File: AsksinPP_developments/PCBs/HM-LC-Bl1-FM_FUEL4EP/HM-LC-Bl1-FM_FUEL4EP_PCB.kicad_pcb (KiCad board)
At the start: 2 copper layers, 124.5 x 96.7 mm, 68 parts, among them J1 Down Button, J10 charge, J11 24V PSU, J12 230V Netzteil Relais, J13 Velux Motor, J14 Motor direction LEDs, J15 Charge Indication LED, J16 H Brücke Relais In, J17 Motor Relais In, J18 Conn_01x03, J2 Up Button, J3 Dual LED, J4 Config Button, J5 ISP Programmer, J6 Accumulator, J7 LED rot, J8 LED grün, J9 LED gelb, Q1 IRLU024N, Q2 BD238, Q3 IRF9Z34N, Q4 2N7000, Q5 MCP1702-2802E_TO

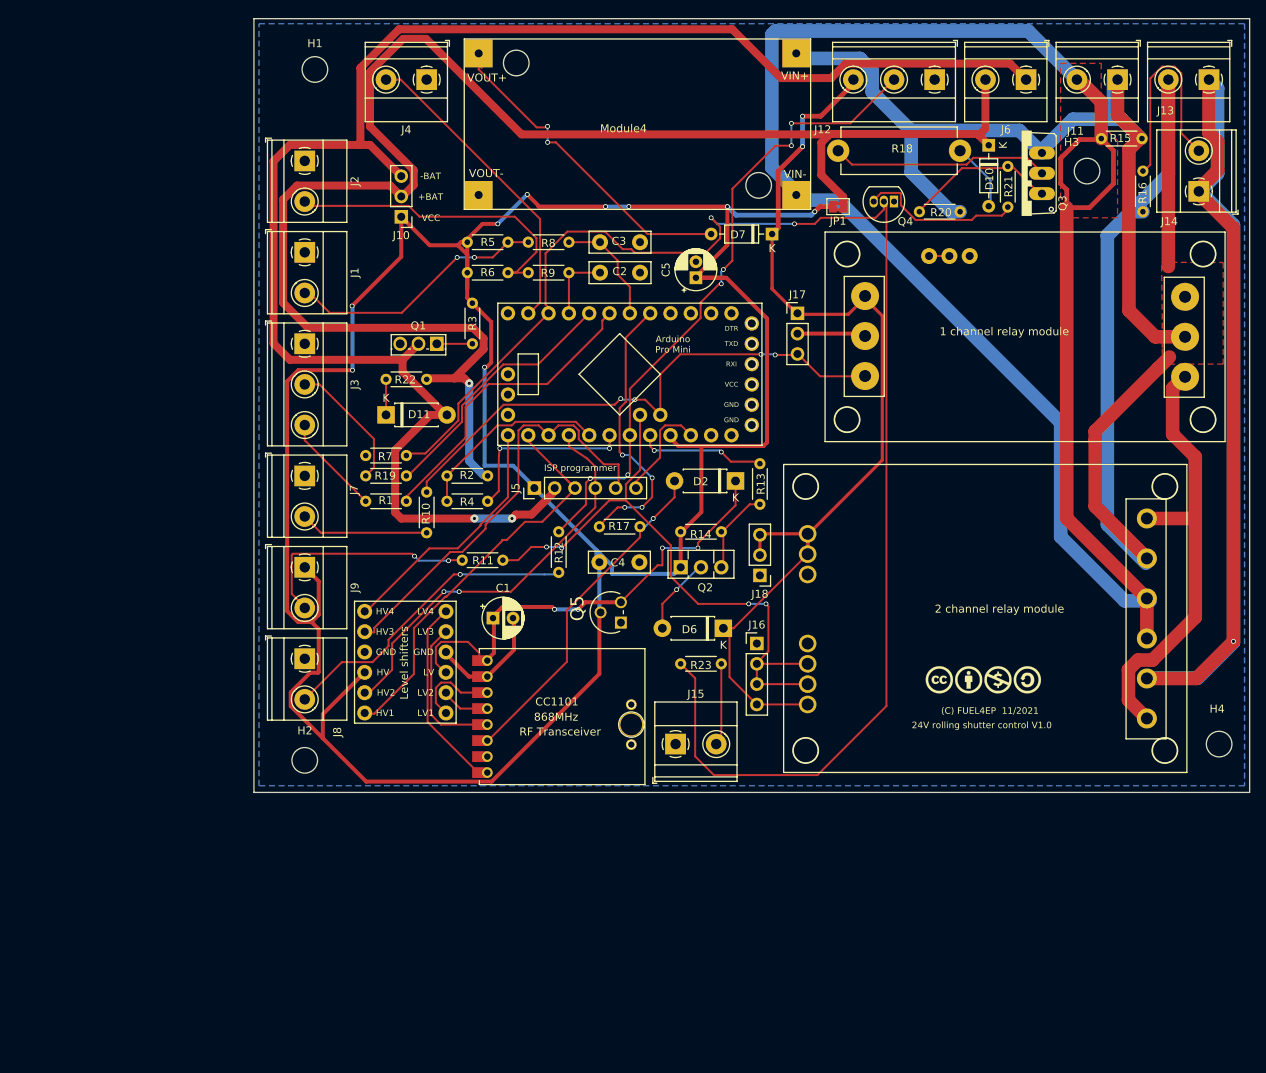
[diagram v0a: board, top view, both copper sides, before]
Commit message: PCBs/HB-UNI-SenAct-4-4-SC_DS_FUEL4EP and PCBs/HM-LC-Bl1-FM_FUEL4EP: fixes of some geometry flaws that popped up during trial assembly
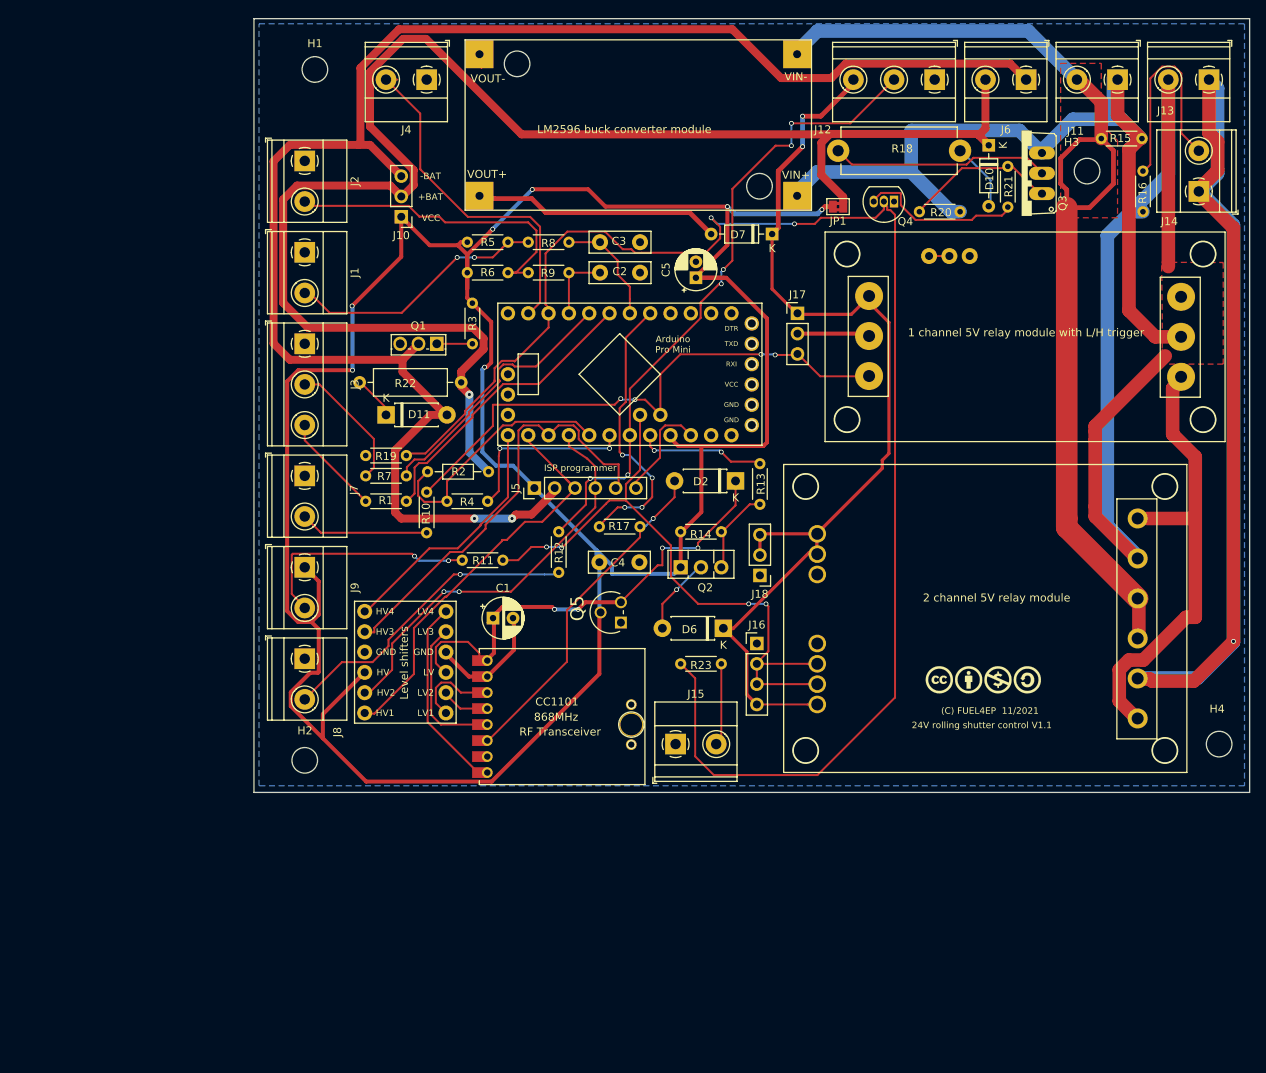
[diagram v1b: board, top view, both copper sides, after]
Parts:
- removed Module4: LM2596_buck 24V->6.3V, FUEL4EP:LM2596_buck
- added LM2596 buck converter module: LM2596_buck 24V->6.3V, FUEL4EP:LM2596_buck, F.Cu at (55.6, -30.4)
- 1 channel 5V relay module with L/H trigger: renamed from 1 channel relay module
- 2 channel 5V relay module: renamed from 2 channel relay module
- R2: footprint Resistor_THT:R_Axial_DIN0204_L3.6mm_D1.6mm_P5.08mm_Horizontal -> Resistor_THT:R_Axial_DIN0204_L3.6mm_D1.6mm_P7.62mm_Horizontal
- R22: footprint Resistor_THT:R_Axial_DIN0204_L3.6mm_D1.6mm_P5.08mm_Horizontal -> Resistor_THT:R_Axial_DIN0309_L9.0mm_D3.2mm_P12.70mm_Horizontal
- moved R22 4.33 mm to (55.1, 12.4)
- moved R2 2.48 mm to (50.9, 23.6)
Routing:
- net /GND_power: track 228.0 -> 130.8 mm
- net Net-(D7-Pad2): track 42.0 -> 33.4 mm, vias 2 -> 0
- net /A0: track 24.1 -> 31.6 mm
- net /V_relais: track 125.5 -> 131.2 mm
- net /plusBAT: track 200.7 -> 195.2 mm
- net Net-(J4-Pad2): track 38.8 -> 43.8 mm
- net /24V_raw: track 109.7 -> 105.9 mm
- net /Motor_minus: track 172.2 -> 175.0 mm
- net /A4: track 78.7 -> 81.1 mm
- net /D7: track 188.5 -> 190.7 mm
- net /Motor_plus: track 127.1 -> 125.4 mm
- net /24V_switched: track 56.2 -> 57.7 mm
- net VCC: track 352.6 -> 351.3 mm, vias 9 -> 7
- net /A5: track 68.4 -> 69.6 mm
- net GND: track 22.5 -> 23.6 mm
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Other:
- board text added: "(C) FUEL4EP 11/2021 24V rolling shutter control V1.1"
- board text added: "24V rolling shutter control V1.1"
- board text removed: "(C) FUEL4EP 11/2021 24V rolling shutter control V1.0"
- board text removed: "24V rolling shutter control V1.0"

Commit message: PCBs/HM-LC-Bl1-FM_FUEL4EP and PCBs/HB-UNI-SenAct-4-4-SC_DS_FUEL4EP: fixes, new V1.2 PCB layouts
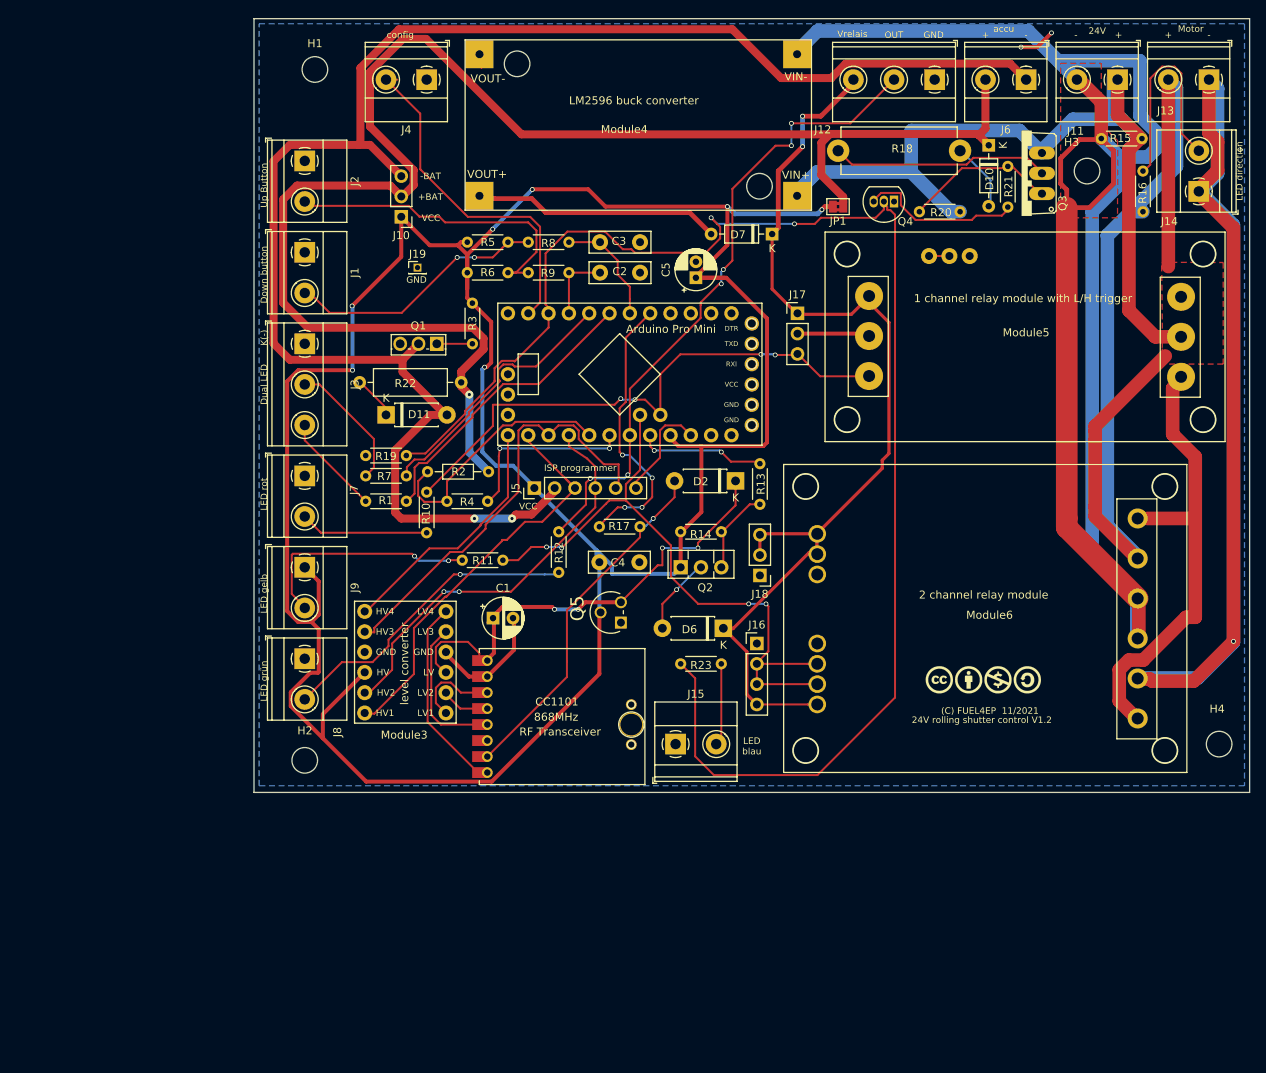
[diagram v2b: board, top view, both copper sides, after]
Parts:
- added J19: GND, Connector_PinHeader_1.27mm:PinHeader_1x01_P1.27mm_Vertical, F.Cu at (49.7, -1.91)
- Module3: renamed from Level shifters; value 4_channel_LOGIC_LEVEL_CONVERTER -> >VALUE
- Module4: renamed from LM2596 buck converter module
- Module5: renamed from 1 channel 5V relay module with L/H trigger
- Module6: renamed from 2 channel 5V relay module
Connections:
- Module2 pad 6C: Net-(D2-Pad2) -> Net-(Module2-Pad6C)
- Module2 pad 7C: Net-(Module2-Pad7C) -> Net-(D2-Pad2)
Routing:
- net /GND_power: track 130.8 -> 225.1 mm
- net GND: track 23.6 -> 28.1 mm, vias 0 -> 2
- net Net-(D2-Pad2): track 44.1 -> 47.5 mm
- net Net-(Module2-Pad7C): track 1.19 -> 0.00 mm
- net Net-(Module2-Pad6C): track 0.00 -> 1.00 mm
- net /Motor_plus: track 125.4 -> 126.2 mm
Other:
- board text added: "(C) FUEL4EP 11/2021 24V rolling shutter control V1.2"
- board text added: "+"
- board text added: "-"
- board text added: "24V"
- board text added: "24V rolling shutter control V1.2"
- board text added: "Down button"
- board text added: "Dual LED"
- board text added: "GND"
- board text added: "K(-)"
- board text added: "LED blau"
- board text added: "LED direction"
- board text added: "LED gelb"
- board text added: "LED grün"
- board text added: "LED rot"
- board text added: "Motor"
- board text added: "OUT"
- board text added: "Up Button"
- board text added: "Vrelais"
- board text added: "accu"
- board text added: "config"
- board text removed: "(C) FUEL4EP 11/2021 24V rolling shutter control V1.1"
- board text removed: "24V rolling shutter control V1.1"
- board text removed: "Arduino Pro Mini"

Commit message: PCBs/HM-LC-Bl1-FM_FUEL4EP: fix of R18
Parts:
- Module3: value >VALUE -> 4_channel_LOGIC_LEVEL_CONVERTER
- R18: value 22 -> 180

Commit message: PCBs/HB-UNI-SenAct-4-4-SC_DS_FUEL4EP and PCBs/HM-LC-Bl1-FM_FUEL4EP: fix of R2 to 470kOhm
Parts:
- R2: value 200k -> 470k

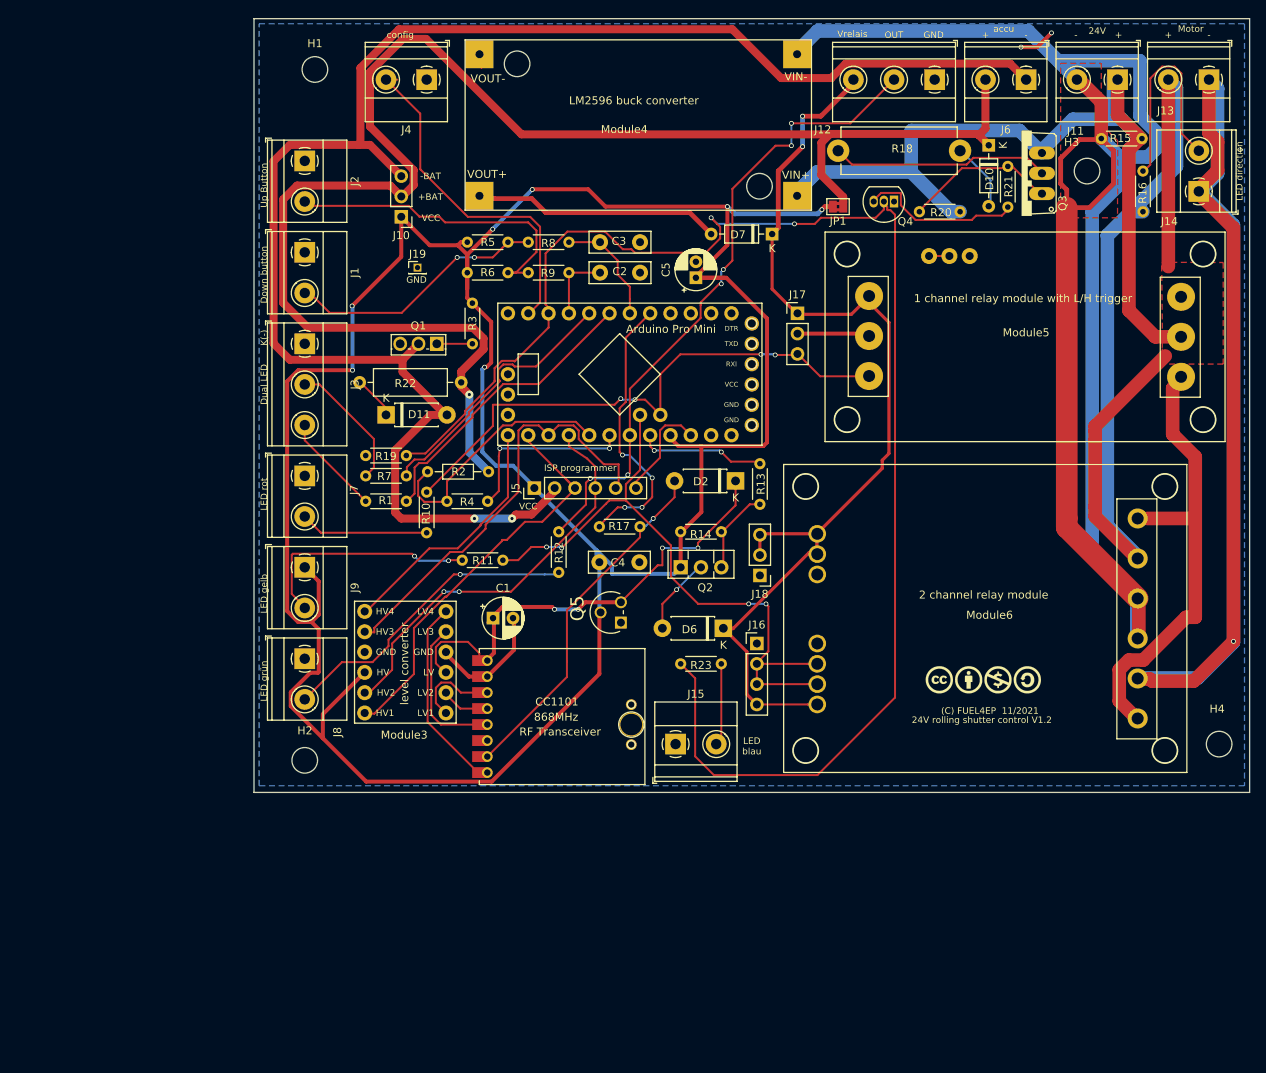
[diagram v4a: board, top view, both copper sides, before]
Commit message: major update: hb-ep-devices-addon V1.14; added sketches HB-UNI-Sensor1-AQ-BME680_KF_rLF and HB-UNI-SenAct-4-4-SC_DS; migration of all PPCBs to KiCAD 6
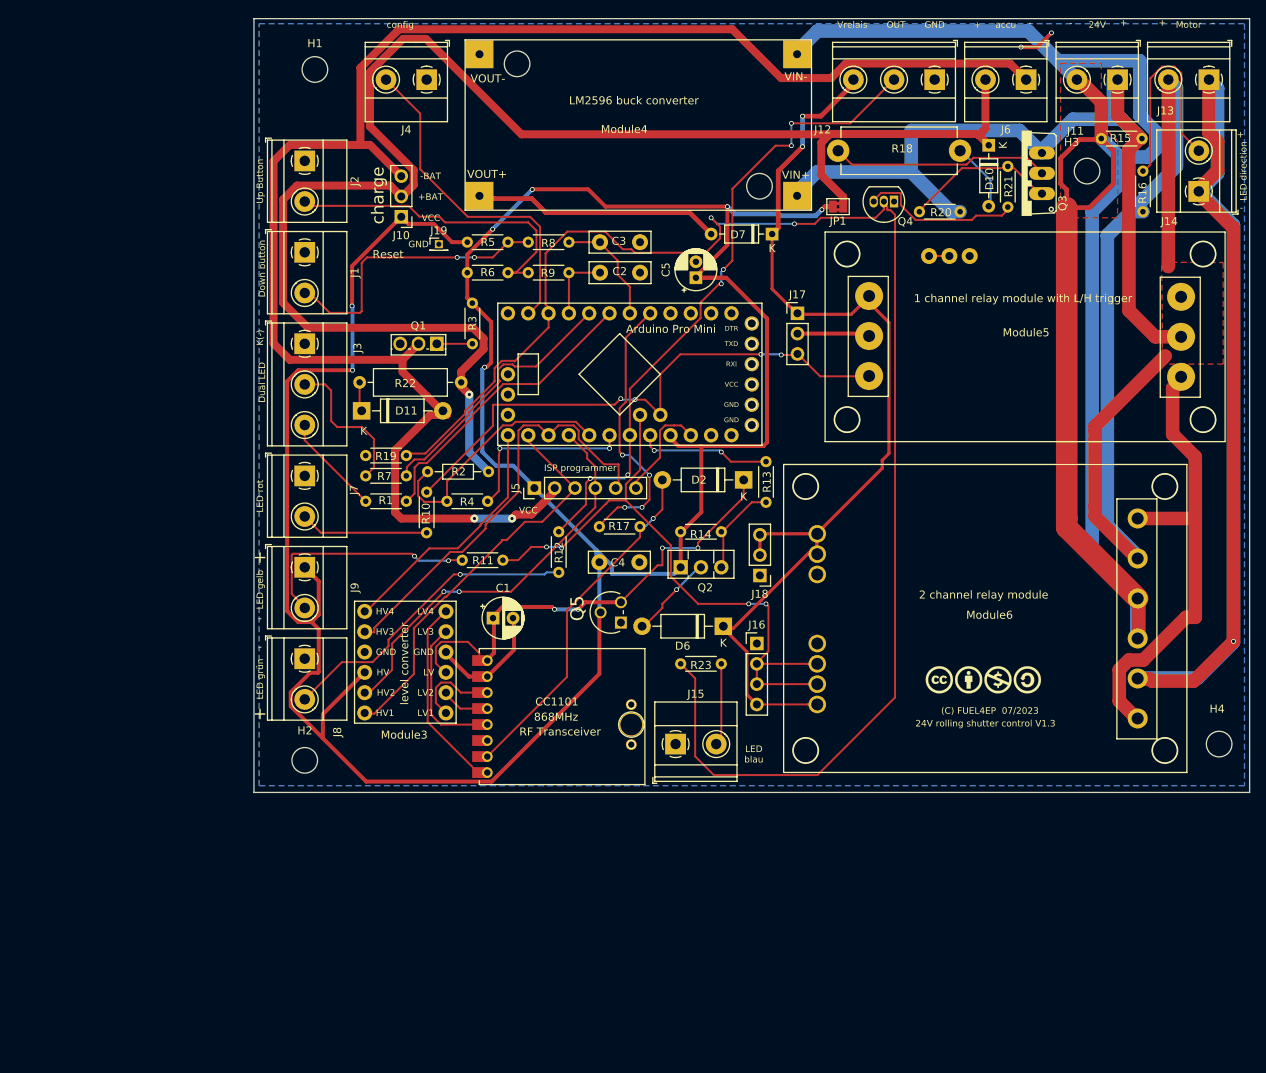
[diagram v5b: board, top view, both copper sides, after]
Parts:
- D11, D2, D6: footprint Diode_THT:D_DO-41_SOD81_P7.62mm_Horizontal -> Diode_THT:D_DO-41_SOD81_P10.16mm_Horizontal
- Module3: value 4_channel_LOGIC_LEVEL_CONVERTER -> >VALUE
- moved J19 3.96 mm to (52.3, -4.83)
- moved D11 3.09 mm to (42.7, 16.0)
- moved D2 1.02 mm to (90.4, 24.6)
- moved R13 0.80 mm to (93.2, 22.4)
- moved D6 0.25 mm to (87.9, 42.9)
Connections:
- Module1 pad 12C: Net-(Module1-Pad12C) -> unconnected-(Module1-Pad12C)
- Module1 pad 1A: Net-(Module1-Pad1A) -> unconnected-(Module1-Pad1A)
- Module1 pad 1C: Net-(Module1-Pad1C) -> unconnected-(Module1-Pad1C)
- Module1 pad 1D: Net-(Module1-Pad1D) -> unconnected-(Module1-Pad1D)
- Module1 pad 2B: Net-(Module1-Pad2B) -> unconnected-(Module1-Pad2B)
- Module1 pad 2C: Net-(Module1-Pad2C) -> unconnected-(Module1-Pad2C)
- Module1 pad 2D: Net-(Module1-Pad2D) -> unconnected-(Module1-Pad2D)
- Module1 pad 3B: Net-(Module1-Pad3B) -> unconnected-(Module1-Pad3B)
- Module1 pad 3C: Net-(Module1-Pad3C) -> unconnected-(Module1-Pad3C)
- Module1 pad 3D: Net-(Module1-Pad3D) -> unconnected-(Module1-Pad3D)
- Module1 pad 4C: Net-(Module1-Pad4C) -> unconnected-(Module1-Pad4C)
- Module1 pad 4D: Net-(Module1-Pad4D) -> unconnected-(Module1-Pad4D)
- Module1 pad 5D: Net-(Module1-Pad5D) -> unconnected-(Module1-Pad5D)
- Module1 pad 6D: Net-(Module1-Pad6D) -> unconnected-(Module1-Pad6D)
- Module2 pad 2A: Net-(Module2-Pad2A) -> unconnected-(Module2-Pad2A)
- Module2 pad 6C: Net-(Module2-Pad6C) -> unconnected-(Module2-Pad6C)
- Module5 pad 1A: Net-(Module5-Pad1A) -> unconnected-(Module5-Pad1A)
- Module5 pad 3D: Net-(Module5-Pad3D) -> unconnected-(Module5-Pad3D)
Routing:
- net VCC: track 351.3 -> 345.3 mm
- net Net-(J1-Pad2): track 32.9 -> 36.4 mm
- net Net-(J3-Pad2): track 16.4 -> 18.7 mm
- net Net-(D11-Pad1): track 5.38 -> 3.66 mm
- net /MOSI: track 52.2 -> 50.5 mm
- net Net-(J4-Pad2): track 43.8 -> 42.4 mm
- net GND: track 28.1 -> 27.0 mm
- net unconnected-(Module2-Pad6C): track 0.00 -> 1.00 mm
- net Net-(Module2-Pad6C): track 1.00 -> 0.00 mm
- net Net-(D6-Pad2): track 9.51 -> 10.5 mm
- net /SCK: track 50.6 -> 49.8 mm
- net Net-(Q2-Pad3): track 10.3 -> 11.1 mm
- net /LDO_3.3V: track 60.8 -> 59.9 mm
- net /RSET: track 13.7 -> 13.1 mm
- net Net-(D2-Pad2): track 47.5 -> 46.9 mm
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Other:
- net class Default removed
- net class battery removed
- net class power removed
- net class supply removed
- board text added: "(C) FUEL4EP 07/2023"
- board text added: "(C) FUEL4EP 07/2023 24V rolling shutter control V1.3"
- board text added: "24V rolling shutter control V1.3"
- board text added: "Reset"
- board text added: "charge"
- board text removed: "(C) FUEL4EP 11/2021"
- board text removed: "(C) FUEL4EP 11/2021 24V rolling shutter control V1.2"
- board text removed: "24V rolling shutter control V1.2"
